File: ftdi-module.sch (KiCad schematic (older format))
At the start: 48 parts, among them J1 USB3106-30-0230-A, U1 FT2232HL-REEL, U7 AP62301WU-7, Y1 KX-7_12,MHz

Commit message: Improvements after review
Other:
- note removed: "REMARK: Missing symbol"
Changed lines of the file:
@@
 Wire Wire Line
 	2450 2200 2450 2250
-$Comp
-L nuc-compute-cluster-power-breakout:Logo_Open_Hardware_Large #LOGO1
-U 1 1 622C2468
-P 15350 9550
-F 0 "#LOGO1" H 15350 10050 50  0001 C CNN
-F 1 "Logo_Open_Hardware_Large" H 15350 9150 50  0001 C CNN
-F 2 "" H 15350 9550 50  0001 C CNN
-F 3 "~" H 15350 9550 50  0001 C CNN
-	1    15350 9550
-	1    0    0    -1
-$EndComp
 NoConn ~ 5400 5450
 NoConn ~ 5400 5350
@@
 Text Notes 7700 4600 0    79   ~ 0
 I2C Pull-Ups
-Text Notes 14250 9175 0    79   ~ 0
-REMARK: Missing symbol
-Text Notes 9000 4650 0    79   ~ 0
+Text Notes 13650 4800 0    79   ~ 0
 TODO: What is the scenario for 5V0 \npower supply without the 12V? \nAdd 0R in the same place as D3 \nand mark D3 and D4 as DNP.
 $EndSCHEMATC

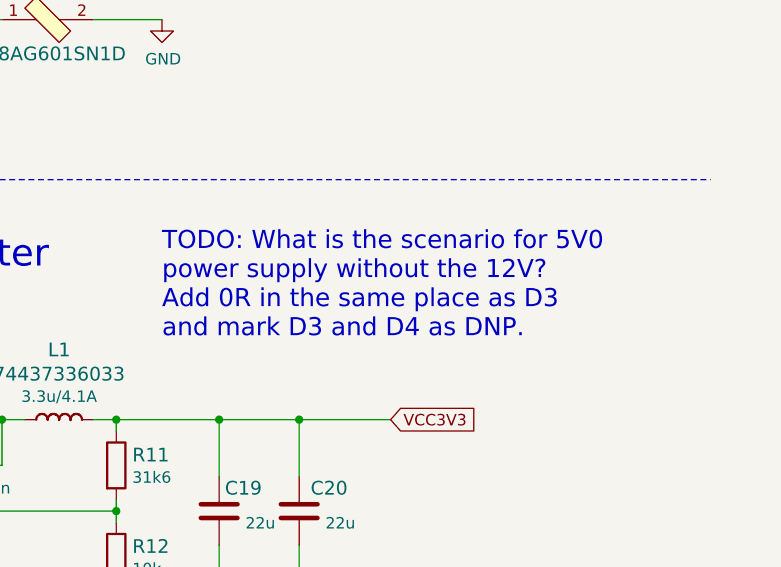
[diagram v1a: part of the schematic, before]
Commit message: Add remarks to the schematic
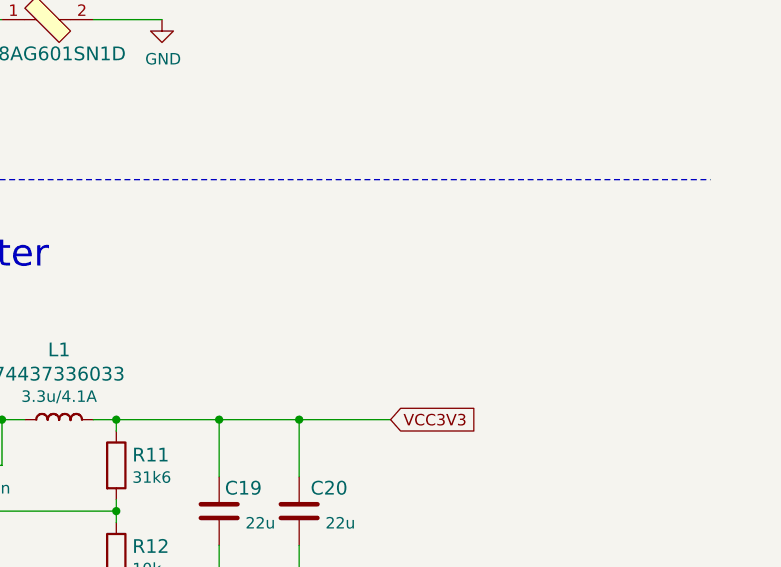
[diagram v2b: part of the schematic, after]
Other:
- note removed: "TODO: What is the scenario for 5V0 \npower supply without the 12V? \nAdd 0R in the same place as D3 \nand mark D3 and D4 as DNP."
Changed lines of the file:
@@
 Text Notes 7700 4600 0    79   ~ 0
 I2C Pull-Ups
-Text Notes 13650 4800 0    79   ~ 0
-TODO: What is the scenario for 5V0 \npower supply without the 12V? \nAdd 0R in the same place as D3 \nand mark D3 and D4 as DNP.
 $EndSCHEMATC

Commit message: Galvanic isolation implementation
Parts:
- removed C16: C_10u_16V_0603, nuc-compute-cluster-power-breakout-footprints:0603-cap, symbol nuc-compute-cluster-power-breakout:C_10u_16V_0603
- removed C18: C_100n_0402, nuc-compute-cluster-power-breakout-footprints:0402-cap, symbol nuc-compute-cluster-power-breakout:C_100n_0402
- removed C19, C20: C_22u_0603, nuc-compute-cluster-power-breakout-footprints:0603-cap, symbol nuc-compute-cluster-power-breakout:C_22u_0603
- removed D3, D4: MBRS330T3G, nuc-compute-cluster-power-breakout-footprints:MBRS340T3, symbol nuc-compute-cluster-power-breakout:MBRS330T3G
- removed L1: 74437336033, nuc-compute-cluster-power-breakout-footprints:WE_74437336033, symbol nuc-compute-cluster-power-breakout:74437336033
- removed R11: R_31k6_0402, nuc-compute-cluster-power-breakout-footprints:0402-res, symbol nuc-compute-cluster-power-breakout:R_31k6_0402
- removed R12: R_10k_0402, nuc-compute-cluster-power-breakout-footprints:0402-res, symbol nuc-compute-cluster-power-breakout:R_10k_0402
- removed R36, R37: R_4k7_0402, nuc-compute-cluster-power-breakout-footprints:0402-res, symbol nuc-compute-cluster-power-breakout:R_4k7_0402
- removed U7: AP62301WU-7, nuc-compute-cluster-power-breakout-footprints:TSOT23-6, symbol nuc-compute-cluster-power-breakout:AP62301WU-7
- added 3V3_USB1, SCL_FTDI1, SDA_FTDI1: TP_SMD1MM, nuc-compute-cluster-power-breakout-footprints:Testpoint_smd_1mm, symbol nuc-compute-cluster-power-breakout:TP_SMD1MM
- added C16, C18: C_100n_0402, antmicro-footprints:0402-cap, symbol antmicroCapacitors0402:C_100n_0402
- added C19, C20: C_1u_0402, antmicro-footprints:0402-cap, symbol antmicroCapacitors0402:C_1u_0402
- added R11, R12, R36, R37: R_1k5_0402, antmicro-footprints:0402-res, symbol antmicroResistors0402:R_1k5_0402
- added R38, R39, R42: R_0R_0603, nuc-compute-cluster-power-breakout-footprints:0603-res, symbol nuc-compute-cluster-power-breakout:R_0R_0603
- added U2: ISO1641, antmicro-footprints:SOIC-8_W3.9mm, symbol antmicroOptoisolatorsLogicOutput:ISO1641
- added U3: NCP163ASN330T1G, antmicro-footprints:SOT-23-5, symbol antmicroPMICVoltageRegulatorsLinear:NCP163ASN330T1G
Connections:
- net GND: now also C18.2, R42.2, U2.5 (GND2); no longer C1.2, C10.2, C11.2, C12.2, C13.2, C14.2, C15.2, C17.2, C2.2, C3.2, C4.2, C5.2, C6.2, C7.2, C8.2, C9.2, D1.3 (GND), D2.2, FB3.2, J1.5, R2.2, R3.1, R6.2, U1.1 (GND), U1.10 (AGND), U1.11 (GND), U1.13 (TEST), U1.15 (GND), U1.25 (GND), U1.35 (GND), U1.47 (GND), U1.5 (GND), U1.51 (GND), Y1.2, Y1.4
- net SCL: now also R36.2, R39.2, U2.6 (SCL2)
- net SDA: now also R37.2, R38.2, U2.7 (SDA2)
- net VCC3V3: now also C18.1, R36.1, R37.1, U2.8 (VCC2); no longer C3.1, C4.1, C5.1, C6.1, C7.1, FB1.2, FB2.2, R1.1, R7.1, U1.20 (VCCIO-1), U1.31 (VCCIO-2), U1.42 (VCCIO-3), U1.50 (VREGIN), U1.56 (VCCIO-4)
- net VCC5V0_USB: now also C19.1, U3.1 (VIN), U3.3 (EN)
- new net GNDD: C1.2, C10.2, C11.2, C12.2, C13.2, C14.2, C15.2, C16.2, C17.2, C19.2, C2.2, C20.2, C3.2, C4.2, C5.2, C6.2, C7.2, C8.2, C9.2, D1.3 (GND), D2.2, FB3.2, J1.5, R2.2, R3.1, R42.1, R6.2, U1.1 (GND), U1.10 (AGND), U1.11 (GND), U1.13 (TEST), U1.15 (GND), U1.25 (GND), U1.35 (GND), U1.47 (GND), U1.5 (GND), U1.51 (GND), U2.4 (GND1), U3.2 (GND), Y1.2, Y1.4
- new net SCL_FTDI: R12.2, R39.1, SCL_FTDI1.1, U2.3 (SCL1)
- new net SDA_FTDI: R11.2, R38.1, SDA_FTDI1.1, U2.2 (SDA1)
- new net VCC3V3_USB: 3V3_USB1.1, C16.1, C20.1, C3.1, C4.1, C5.1, C6.1, C7.1, FB1.2, FB2.2, R1.1, R11.1, R12.1, R7.1, U1.20 (VCCIO-1), U1.31 (VCCIO-2), U1.42 (VCCIO-3), U1.50 (VREGIN), U1.56 (VCCIO-4), U2.1 (VCC1), U3.5 (VOUT)
- no-connect marks 7 -> 34
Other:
- note added: "3V3 LDO\n"
- note added: "Filtration"
- note added: "Transmission Lines Separation\n"
- note removed: "3V3 DC/DC Converter"
- note removed: "I2C Pull-Ups"
- moved on the sheet: 3V3, 5V_USB1, C10, C13, C3, C4, C5, C6, C7, C8, C9, D2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

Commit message: Complete galvanic isolated layout
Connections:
- net SCL: no longer R4.2, U1.18 (ADBUS2)
- net SCL_FTDI: now also R4.2, U1.18 (ADBUS2)
- net SDA: no longer U1.16 (ADBUS0)
- net SDA_FTDI: now also U1.16 (ADBUS0)
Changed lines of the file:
@@
 Wire Wire Line
 	5900 4450 5400 4450
-Text GLabel 6650 4150 2    50   Input ~ 0
-SDA
-Text GLabel 6650 4350 2    50   Input ~ 0
-SCL
+Text GLabel 6650 4150 2    50   BiDi ~ 0
+SDA_FTDI
+Text GLabel 6650 4350 2    50   Output ~ 0
+SCL_FTDI
 Connection ~ 6050 4350
 Text GLabel 6650 4450 2    50   Input ~ 0
@@
 	13425 5150 13750 5150
 $Comp
-L power:GNDD #PWR?
+L power:GNDD #PWR0103
 U 1 1 62A019D8
 P 1950 3900
-F 0 "#PWR?" H 1950 3650 50  0001 C CNN
+F 0 "#PWR0103" H 1950 3650 50  0001 C CNN
 F 1 "GNDD" H 1950 3750 50  0000 C CNN
 F 2 "" H 1950 3900 50  0001 C CNN

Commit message: Performed loclib
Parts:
- C16, C18: footprint antmicro-footprints:0402-cap -> nuc-compute-cluster-power-breakout-footprints:0402-cap; symbol antmicroCapacitors0402:C_100n_0402 -> nuc-compute-cluster-power-breakout:C_100n_0402
- C19, C20: footprint antmicro-footprints:0402-cap -> nuc-compute-cluster-power-breakout-footprints:0402-cap; symbol antmicroCapacitors0402:C_1u_0402 -> nuc-compute-cluster-power-breakout:C_1u_0402
- R11, R12, R36, R37: footprint antmicro-footprints:0402-res -> nuc-compute-cluster-power-breakout-footprints:0402-res; symbol antmicroResistors0402:R_1k5_0402 -> nuc-compute-cluster-power-breakout:R_1k5_0402
- U2: footprint antmicro-footprints:SOIC-8_W3.9mm -> nuc-compute-cluster-power-breakout-footprints:SOIC-8_W3.9mm; symbol antmicroOptoisolatorsLogicOutput:ISO1641 -> nuc-compute-cluster-power-breakout:ISO1641
- U3: footprint antmicro-footprints:SOT-23-5 -> nuc-compute-cluster-power-breakout-footprints:SOT-23-5; symbol antmicroPMICVoltageRegulatorsLinear:NCP163ASN330T1G -> nuc-compute-cluster-power-breakout:NCP163ASN330T1G
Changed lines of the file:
@@
 	8950 550  8950 11200
 $Comp
-L antmicroOptoisolatorsLogicOutput:ISO1641 U2
+L nuc-compute-cluster-power-breakout:ISO1641 U2
 U 1 1 6256AE7A
 P 3100 9225
 F 0 "U2" H 3100 9665 50  0000 C CNN
 F 1 "ISO1641" H 3100 9574 50  0000 C CNN
-F 2 "antmicro-footprints:SOIC-8_W3.9mm" H 3100 9225 50  0001 C CNN
+F 2 "nuc-compute-cluster-power-breakout-footprints:SOIC-8_W3.9mm" H 3100 9225 50  0001 C CNN
 F 3 "https://www.ti.com/lit/ds/symlink/iso1641.pdf?ts=1649669035432&ref_url=https%253A%252F%252Fwww.ti.com%252Fproduct%252FISO1641" H 3100 9225 50  0001 C CNN
 F 4 "ISO1641BDR" H 3100 9225 50  0001 C CNN "MPN"
@@
 SCL_FTDI
 $Comp
-L antmicroCapacitors0402:C_100n_0402 C16
+L nuc-compute-cluster-power-breakout:C_100n_0402 C16
 U 1 1 625BE0B8
 P 6775 9250
 F 0 "C16" H 6575 9350 60  0000 L CNN
 F 1 "C_100n_0402" H 6775 9100 60  0001 C CNN
-F 2 "antmicro-footprints:0402-cap" H 6975 9450 60  0001 L CNN
+F 2 "nuc-compute-cluster-power-breakout-footprints:0402-cap" H 6975 9450 60  0001 L CNN
 F 3 "" H 6775 9250 50  0001 C CNN
 F 4 "Murata" H 6975 9650 60  0001 L CNN "Manufacturer"
@@
 $EndComp
 $Comp
-L antmicroCapacitors0402:C_100n_0402 C18
+L nuc-compute-cluster-power-breakout:C_100n_0402 C18
 U 1 1 625BEE93
 P 7200 9250
 F 0 "C18" H 7225 9350 60  0000 L CNN
 F 1 "C_100n_0402" H 7200 9100 60  0001 C CNN
-F 2 "antmicro-footprints:0402-cap" H 7400 9450 60  0001 L CNN
+F 2 "nuc-compute-cluster-power-breakout-footprints:0402-cap" H 7400 9450 60  0001 L CNN
 F 3 "" H 7200 9250 50  0001 C CNN
 F 4 "Murata" H 7400 9650 60  0001 L CNN "Manufacturer"
@@
 VCC3V3_USB
 $Comp
-L power:GNDD #PWR06
+L nuc-compute-cluster-power-breakout:GNDD #PWR06
 U 1 1 625D2321
 P 2575 9625
@@
 	2100 9275 2400 9275
 $Comp
-L antmicroResistors0402:R_1k5_0402 R11
+L nuc-compute-cluster-power-breakout:R_1k5_0402 R11
 U 1 1 62622E8A
 P 2300 8900
 F 0 "R11" V 2250 8675 60  0000 L CNN
 F 1 "R_1k5_0402" H 2300 8750 60  0001 C CNN
-F 2 "antmicro-footprints:0402-res" H 2500 9100 60  0001 L CNN
+F 2 "nuc-compute-cluster-power-breakout-footprints:0402-res" H 2500 9100 60  0001 L CNN
 F 3 "" H 2300 8900 50  0001 C CNN
 F 4 "Multicomp Pro" H 2500 9300 60  0001 L CNN "Manufacturer"
@@
 $EndComp
 $Comp
-L antmicroResistors0402:R_1k5_0402 R12
+L nuc-compute-cluster-power-breakout:R_1k5_0402 R12
 U 1 1 62622622
 P 2400 8900
 F 0 "R12" V 2350 8950 60  0000 L CNN
 F 1 "R_1k5_0402" H 2400 8750 60  0001 C CNN
-F 2 "antmicro-footprints:0402-res" H 2600 9100 60  0001 L CNN
+F 2 "nuc-compute-cluster-power-breakout-footprints:0402-res" H 2600 9100 60  0001 L CNN
 F 3 "" H 2400 8900 50  0001 C CNN
 F 4 "Multicomp Pro" H 2600 9300 60  0001 L CNN "Manufacturer"
@@
 	3600 8575 3600 9025
 $Comp
-L antmicroResistors0402:R_1k5_0402 R37
+L nuc-compute-cluster-power-breakout:R_1k5_0402 R37
 U 1 1 6266ECEE
 P 3975 8900
 F 0 "R37" V 3925 8975 60  0000 L CNN
 F 1 "R_1k5_0402" H 3975 8750 60  0001 C CNN
-F 2 "antmicro-footprints:0402-res" H 4175 9100 60  0001 L CNN
+F 2 "nuc-compute-cluster-power-breakout-footprints:0402-res" H 4175 9100 60  0001 L CNN
 F 3 "" H 3975 8900 50  0001 C CNN
 F 4 "Multicomp Pro" H 4175 9300 60  0001 L CNN "Manufacturer"
@@
 $EndComp
 $Comp
-L antmicroResistors0402:R_1k5_0402 R36
+L nuc-compute-cluster-power-breakout:R_1k5_0402 R36
 U 1 1 6266F027
 P 3875 8900
 F 0 "R36" V 3825 8675 60  0000 L CNN
 F 1 "R_1k5_0402" H 3875 8750 60  0001 C CNN
-F 2 "antmicro-footprints:0402-res" H 4075 9100 60  0001 L CNN
+F 2 "nuc-compute-cluster-power-breakout-footprints:0402-res" H 4075 9100 60  0001 L CNN
 F 3 "" H 3875 8900 50  0001 C CNN
 F 4 "Multicomp Pro" H 4075 9300 60  0001 L CNN "Manufacturer"
@@
 $EndComp
 $Comp
-L power:GNDD #PWR028
+L nuc-compute-cluster-power-breakout:GNDD #PWR028
 U 1 1 626C30A0
 P 6775 9550
@@
 	7200 9550 7200 9400
 $Comp
-L power:GNDD #PWR021
+L nuc-compute-cluster-power-breakout:GNDD #PWR021
 U 1 1 62712903
 P 6250 7575
@@
 $EndComp
 $Comp
-L power:GNDD #PWR018
+L nuc-compute-cluster-power-breakout:GNDD #PWR018
 U 1 1 627139AC
 P 5900 7575
@@
 $EndComp
 $Comp
-L power:GNDD #PWR017
+L nuc-compute-cluster-power-breakout:GNDD #PWR017
 U 1 1 62713DC5
 P 5550 7575
@@
 $EndComp
 $Comp
-L power:GNDD #PWR015
+L nuc-compute-cluster-power-breakout:GNDD #PWR015
 U 1 1 62714060
 P 5250 7575
@@
 	6250 7300 6250 7575
 $Comp
-L power:GNDD #PWR014
+L nuc-compute-cluster-power-breakout:GNDD #PWR014
 U 1 1 6273E00B
 P 4000 7575
@@
 $EndComp
 $Comp
-L power:GNDD #PWR013
+L nuc-compute-cluster-power-breakout:GNDD #PWR013
 U 1 1 6273E42F
 P 3700 7575
@@
 $EndComp
 $Comp
-L power:GNDD #PWR011
+L nuc-compute-cluster-power-breakout:GNDD #PWR011
 U 1 1 6273E961
 P 3400 7575
@@
 $EndComp
 $Comp
-L power:GNDD #PWR010
+L nuc-compute-cluster-power-breakout:GNDD #PWR010
 U 1 1 6273EC83
 P 3100 7575
@@
 $EndComp
 $Comp
-L power:GNDD #PWR08
+L nuc-compute-cluster-power-breakout:GNDD #PWR08
 U 1 1 6273EF38
 P 2800 7575
@@
 	4000 7300 4000 7575
 $Comp
-L power:GNDD #PWR016
+L nuc-compute-cluster-power-breakout:GNDD #PWR016
 U 1 1 62774F8D
 P 5550 6175
@@
 	5550 5950 5550 6175
 $Comp
-L power:GNDD #PWR024
+L nuc-compute-cluster-power-breakout:GNDD #PWR024
 U 1 1 6278D604
 P 6400 5025
@@
 	6400 4800 6400 5025
 $Comp
-L power:GNDD #PWR039
+L nuc-compute-cluster-power-breakout:GNDD #PWR039
 U 1 1 628153AF
 P 11400 3400
@@
 $EndComp
 $Comp
-L power:GNDD #PWR072
+L nuc-compute-cluster-power-breakout:GNDD #PWR072
 U 1 1 628171AE
 P 12200 3400
@@
 $EndComp
 $Comp
-L power:GNDD #PWR078
+L nuc-compute-cluster-power-breakout:GNDD #PWR078
 U 1 1 628174B3
 P 13650 3400
@@
 $EndComp
 $Comp
-L power:GNDD #PWR038
+L nuc-compute-cluster-power-breakout:GNDD #PWR038
 U 1 1 628183E7
 P 10750 2350
@@
 $EndComp
 $Comp
-L power:GNDD #PWR02
+L nuc-compute-cluster-power-breakout:GNDD #PWR02
 U 1 1 62824B74
 P 1950 4950
@@
 $EndComp
 $Comp
-L power:GNDD #PWR03
+L nuc-compute-cluster-power-breakout:GNDD #PWR03
 U 1 1 62825BEB
 P 2250 4950
@@
 $EndComp
 $Comp
-L power:GNDD #PWR05
+L nuc-compute-cluster-power-breakout:GNDD #PWR05
 U 1 1 62825E96
 P 2550 4950
@@
 $EndComp
 $Comp
-L power:GNDD #PWR07
+L nuc-compute-cluster-power-breakout:GNDD #PWR07
 U 1 1 628275CD
 P 2750 2250
@@
 $EndComp
 $Comp
-L power:GNDD #PWR04
+L nuc-compute-cluster-power-breakout:GNDD #PWR04
 U 1 1 6282A8E7
 P 2450 2250
@@
 $EndComp
 $Comp
-L power:GNDD #PWR09
+L nuc-compute-cluster-power-breakout:GNDD #PWR09
 U 1 1 6282ABD3
 P 3000 2250
@@
 $EndComp
 $Comp
-L power:GNDD #PWR037
+L nuc-compute-cluster-power-breakout:GNDD #PWR037
 U 1 1 6282B906
 P 10625 9125
@@
 	6000 3150 6000 3250
 $Comp
-L power:GNDD #PWR019
+L nuc-compute-cluster-power-breakout:GNDD #PWR019
 U 1 1 62838EB1
 P 6000 3250
@@
 $EndComp
 $Comp
-L power:GNDD #PWR020
+L nuc-compute-cluster-power-breakout:GNDD #PWR020
 U 1 1 62839261
 P 6200 3250
@@
 $EndComp
 $Comp
-L power:GNDD #PWR022
+L nuc-compute-cluster-power-breakout:GNDD #PWR022
 U 1 1 6283968A
 P 6400 3250
@@
 $EndComp
 $Comp
-L power:GNDD #PWR026
+L nuc-compute-cluster-power-breakout:GNDD #PWR026
 U 1 1 62839A67
 P 6600 3250
@@
 $EndComp
 $Comp
-L power:GNDD #PWR029
+L nuc-compute-cluster-power-breakout:GNDD #PWR029
 U 1 1 628E793A
 P 6775 10575
@@
 	2625 9025 2625 8575
 $Comp
-L antmicroPMICVoltageRegulatorsLinear:NCP163ASN330T1G U3
+L nuc-compute-cluster-power-breakout:NCP163ASN330T1G U3
 U 1 1 629428B6
 P 12775 5200
 F 0 "U3" H 12775 5499 50  0000 C CNN
 F 1 "NCP163ASN330T1G" H 12775 5416 39  0000 C CNN
-F 2 "antmicro-footprints:SOT-23-5" H 12775 4950 50  0001 C CNN
+F 2 "nuc-compute-cluster-power-breakout-footprints:SOT-23-5" H 12775 4950 50  0001 C CNN
 F 3 "https://pl.mouser.com/datasheet/2/308/1/NCP163_D-2317108.pdf" H 12875 5550 50  0001 C CNN
 F 4 "NCP163ASN330T1G" H 12625 5500 50  0001 C CNN "MPN"
@@
 $EndComp
 $Comp
-L antmicroCapacitors0402:C_1u_0402 C19
+L nuc-compute-cluster-power-breakout:C_1u_0402 C19
 U 1 1 6294BBE2
 P 11925 5400
 F 0 "C19" H 11700 5500 60  0000 L CNN
 F 1 "C_1u_0402" H 11925 5250 60  0001 C CNN
-F 2 "antmicro-footprints:0402-cap" H 12125 5600 60  0001 L CNN
+F 2 "nuc-compute-cluster-power-breakout-footprints:0402-cap" H 12125 5600 60  0001 L CNN
 F 3 "" H 11925 5400 50  0001 C CNN
 F 4 "TDK" H 12125 5800 60  0001 L CNN "Manufacturer"
@@
 VCC5V0_USB
 $Comp
-L power:GNDD #PWR040
+L nuc-compute-cluster-power-breakout:GNDD #PWR040
 U 1 1 6294E801
 P 11925 5650
@@
 	11925 5650 11925 5550
 $Comp
-L power:GNDD #PWR076
+L nuc-compute-cluster-power-breakout:GNDD #PWR076
 U 1 1 62985896
 P 13225 5625
@@
 	13225 5625 13225 5250
 $Comp
-L antmicroCapacitors0402:C_1u_0402 C20
+L nuc-compute-cluster-power-breakout:C_1u_0402 C20
 U 1 1 629C5142
 P 13425 5375
 F 0 "C20" H 13475 5475 60  0000 L CNN
 F 1 "C_1u_0402" H 13425 5225 60  0001 C CNN
-F 2 "antmicro-footprints:0402-cap" H 13625 5575 60  0001 L CNN
+F 2 "nuc-compute-cluster-power-breakout-footprints:0402-cap" H 13625 5575 60  0001 L CNN
 F 3 "" H 13425 5375 50  0001 C CNN
 F 4 "TDK" H 13625 5775 60  0001 L CNN "Manufacturer"
@@
 Connection ~ 13425 5150
 $Comp
-L power:GNDD #PWR077
+L nuc-compute-cluster-power-breakout:GNDD #PWR077
 U 1 1 629CEF0E
 P 13425 5625
@@
 	13425 5150 13750 5150
 $Comp
-L power:GNDD #PWR0103
+L nuc-compute-cluster-power-breakout:GNDD #PWR0103
 U 1 1 62A019D8
 P 1950 3900

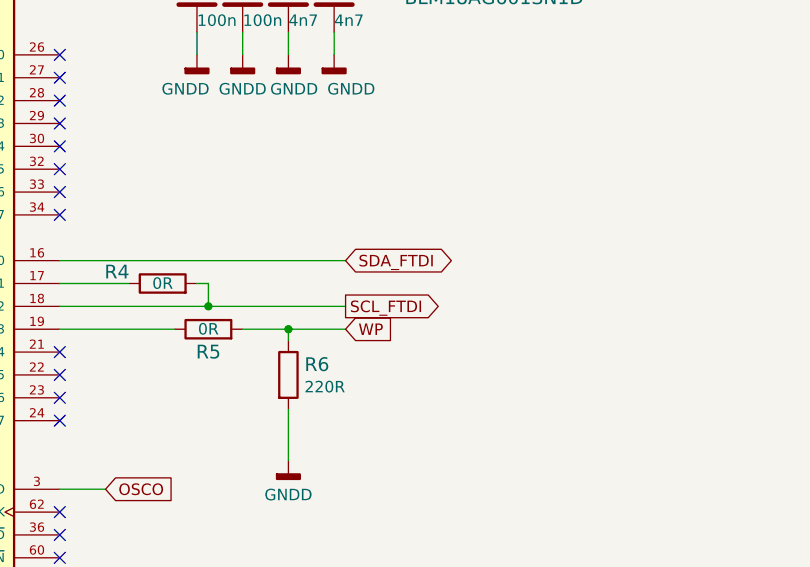
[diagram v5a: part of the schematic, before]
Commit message: Fixed swapped I2C lines Corrected silkscreen layer Rearranged EdgeConn test points
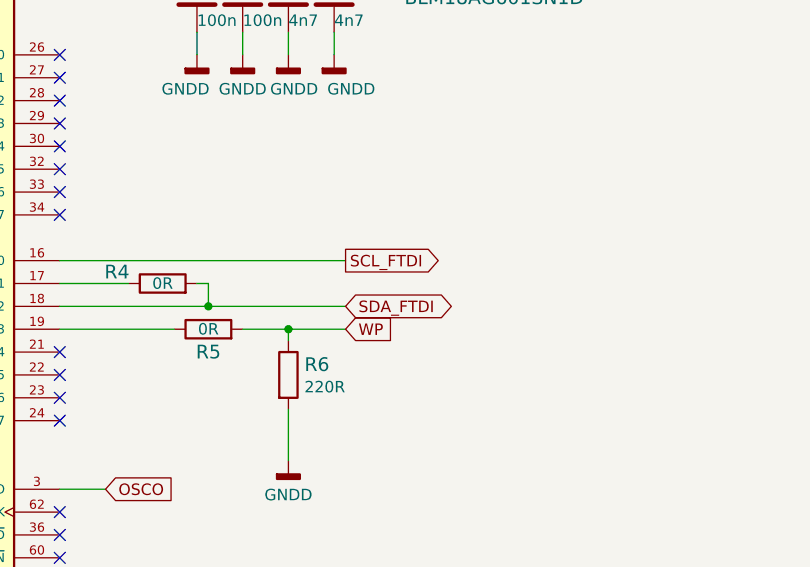
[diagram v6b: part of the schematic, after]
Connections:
- net SCL_FTDI: now also U1.16 (ADBUS0); no longer R4.2, U1.18 (ADBUS2)
- net SDA_FTDI: now also R4.2, U1.18 (ADBUS2); no longer U1.16 (ADBUS0)
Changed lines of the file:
@@
 Wire Wire Line
 	5900 4450 5400 4450
-Text GLabel 6650 4150 2    50   BiDi ~ 0
+Text GLabel 6650 4350 2    50   BiDi ~ 0
 SDA_FTDI
-Text GLabel 6650 4350 2    50   Output ~ 0
+Text GLabel 6650 4150 2    50   Output ~ 0
 SCL_FTDI
 Connection ~ 6050 4350
